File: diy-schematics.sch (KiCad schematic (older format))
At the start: 28 parts, among them J1 CAPSULE, J2 GAINCON, J3 AudioJack2_Ground, J4 USB_SOK, J5 USB_CON, J6 MIC_CON1, J7 MIC_CON2, U1 THAT1512PO8-U1, U2 NMA0515SC

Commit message: new PCB design, some minor compat changes in schematics
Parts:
- removed J3: AudioJack2_Ground, Connector_JST:JST_XH_B2B-XH-A_1x02_P2.50mm_Vertical, symbol Connector:AudioJack2_Ground
- added J3: AUDIO_JACK, Connector_JST:JST_XH_B3B-XH-A_1x03_P2.50mm_Vertical, symbol Connector:Conn_01x03_Female
- C1, C2, C8: footprint Capacitor_SMD:C_0805_2012Metric -> Capacitor_THT:CP_Radial_D5.0mm_P2.00mm
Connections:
- net Earth: now also J3.3 (Pin_3)
- net at C8.2: now also J3.1 (Pin_1), J3.2 (Pin_2)
- net at J4.2 (D-): now also J5.2 (Pin_2); no longer J5.3 (Pin_3)
- net at J4.3 (D+): now also J5.3 (Pin_3); no longer J5.2 (Pin_2)
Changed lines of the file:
@@
 F 0 "C1" V 3552 3950 50  0000 C CNN
 F 1 "22uF" V 3461 3950 50  0000 C CNN
-F 2 "Capacitor_SMD:C_0805_2012Metric" H 3338 3800 50  0001 C CNN
+F 2 "Capacitor_THT:CP_Radial_D5.0mm_P2.00mm" H 3338 3800 50  0001 C CNN
 F 3 "~" H 3300 3950 50  0001 C CNN
 	1    3300 3950
@@
 F 0 "C2" V 3552 4550 50  0000 C CNN
 F 1 "22uF" V 3461 4550 50  0000 C CNN
-F 2 "Capacitor_SMD:C_0805_2012Metric" H 3338 4400 50  0001 C CNN
+F 2 "Capacitor_THT:CP_Radial_D5.0mm_P2.00mm" H 3338 4400 50  0001 C CNN
 F 3 "~" H 3300 4550 50  0001 C CNN
 	1    3300 4550
@@
 F 0 "C8" V 6652 4100 50  0000 C CNN
 F 1 "22uF" V 6561 4100 50  0000 C CNN
-F 2 "Capacitor_SMD:C_0805_2012Metric" H 6438 3950 50  0001 C CNN
+F 2 "Capacitor_THT:CP_Radial_D5.0mm_P2.00mm" H 6438 3950 50  0001 C CNN
 F 3 "~" H 6400 4100 50  0001 C CNN
 	1    6400 4100
@@
 Wire Wire Line
 	3650 3950 4450 3950
-$Comp
-L Connector:AudioJack2_Ground J3
-U 1 1 61D2E7B1
-P 6800 4200
-F 0 "J3" H 6620 4218 50  0000 R CNN
-F 1 "AudioJack2_Ground" H 7050 4500 50  0000 R CNN
-F 2 "Connector_JST:JST_XH_B2B-XH-A_1x02_P2.50mm_Vertical" H 6800 4200 50  0001 C CNN
-F 3 "~" H 6800 4200 50  0001 C CNN
-	1    6800 4200
-	-1   0    0    -1
-$EndComp
 Wire Wire Line
 	6600 4100 6550 4100
@@
 $EndComp
 Wire Wire Line
-	10100 3850 10400 3850
-Wire Wire Line
-	10100 3950 10400 3950
-Wire Wire Line
 	9800 4450 10350 4450
 Wire Wire Line
@@
 	10100 3750 10350 3750
 Connection ~ 10350 3750
+Wire Wire Line
+	10100 3850 10200 3850
+Wire Wire Line
+	10200 3850 10300 3950
+Wire Wire Line
+	10300 3950 10400 3950
+Wire Wire Line
+	10100 3950 10200 3950
+Wire Wire Line
+	10200 3950 10300 3850
+Wire Wire Line
+	10300 3850 10400 3850
+$Comp
+L Connector:Conn_01x03_Female J3
+U 1 1 61D75578
+P 6800 4200
+F 0 "J3" H 6828 4226 50  0000 L CNN
+F 1 "AUDIO_JACK" H 6828 4135 50  0000 L CNN
+F 2 "Connector_JST:JST_XH_B3B-XH-A_1x03_P2.50mm_Vertical" H 6800 4200 50  0001 C CNN
+F 3 "~" H 6800 4200 50  0001 C CNN
+	1    6800 4200
+	1    0    0    -1
+$EndComp
+Wire Wire Line
+	6800 4400 6550 4400
+Wire Wire Line
+	6550 4400 6550 4300
+Wire Wire Line
+	6550 4300 6600 4300
 $EndSCHEMATC

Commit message: fixes to new PCB
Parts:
- removed J3: AUDIO_JACK, Connector_JST:JST_XH_B3B-XH-A_1x03_P2.50mm_Vertical, symbol Connector:Conn_01x03_Female
- added J3: Conn_01x02_Female, Connector_JST:JST_XH_B2B-XH-A_1x02_P2.50mm_Vertical, symbol Connector:Conn_01x02_Female
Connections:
- net Earth: now also J3.2 (Pin_2)
- net at C8.2: now also J3.1 (Pin_1)
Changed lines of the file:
@@
 Wire Wire Line
 	6600 4100 6550 4100
-Wire Wire Line
-	6600 4200 6550 4200
-Wire Wire Line
-	6550 4200 6550 4100
-Connection ~ 6550 4100
 $Comp
 L power:Earth #PWR0110
 U 1 1 61D34EC8
-P 6800 4500
-F 0 "#PWR0110" H 6800 4250 50  0001 C CNN
-F 1 "Earth" H 6800 4350 50  0001 C CNN
-F 2 "" H 6800 4500 50  0001 C CNN
-F 3 "~" H 6800 4500 50  0001 C CNN
-	1    6800 4500
-	1    0    0    -1
-$EndComp
-Wire Wire Line
-	6800 4500 6800 4400
+P 6800 4400
+F 0 "#PWR0110" H 6800 4150 50  0001 C CNN
+F 1 "Earth" H 6800 4250 50  0001 C CNN
+F 2 "" H 6800 4400 50  0001 C CNN
+F 3 "~" H 6800 4400 50  0001 C CNN
+	1    6800 4400
+	1    0    0    -1
+$EndComp
+Wire Wire Line
+	6800 4400 6800 4300
 Connection ~ 8650 4200
 Wire Wire Line
@@
 Wire Wire Line
 	10300 3850 10400 3850
-$Comp
-L Connector:Conn_01x03_Female J3
-U 1 1 61D75578
-P 6800 4200
-F 0 "J3" H 6828 4226 50  0000 L CNN
-F 1 "AUDIO_JACK" H 6828 4135 50  0000 L CNN
-F 2 "Connector_JST:JST_XH_B3B-XH-A_1x03_P2.50mm_Vertical" H 6800 4200 50  0001 C CNN
-F 3 "~" H 6800 4200 50  0001 C CNN
-	1    6800 4200
-	1    0    0    -1
-$EndComp
-Wire Wire Line
-	6800 4400 6550 4400
-Wire Wire Line
-	6550 4400 6550 4300
-Wire Wire Line
-	6550 4300 6600 4300
+Wire Wire Line
+	6800 4300 6550 4300
+Wire Wire Line
+	6550 4300 6550 4200
+Wire Wire Line
+	6550 4200 6600 4200
+$Comp
+L Connector:Conn_01x02_Female J3
+U 1 1 61D275D2
+P 6800 4100
+F 0 "J3" H 6828 4076 50  0000 L CNN
+F 1 "Conn_01x02_Female" H 6828 3985 50  0000 L CNN
+F 2 "Connector_JST:JST_XH_B2B-XH-A_1x02_P2.50mm_Vertical" H 6800 4100 50  0001 C CNN
+F 3 "~" H 6800 4100 50  0001 C CNN
+	1    6800 4100
+	1    0    0    -1
+$EndComp
 $EndSCHEMATC

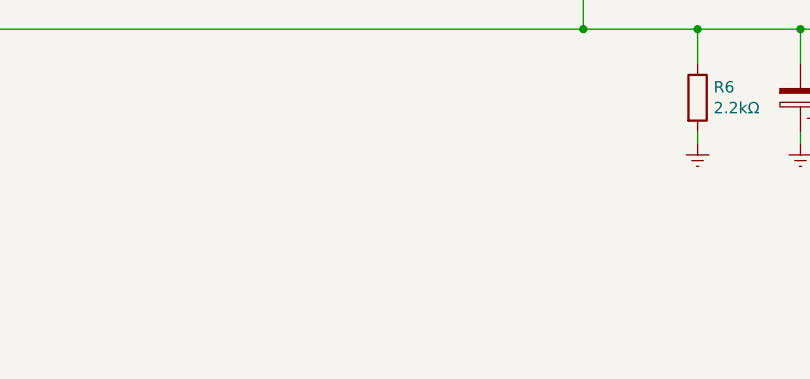
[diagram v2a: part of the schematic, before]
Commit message: added mounting holes, rendered gerber files
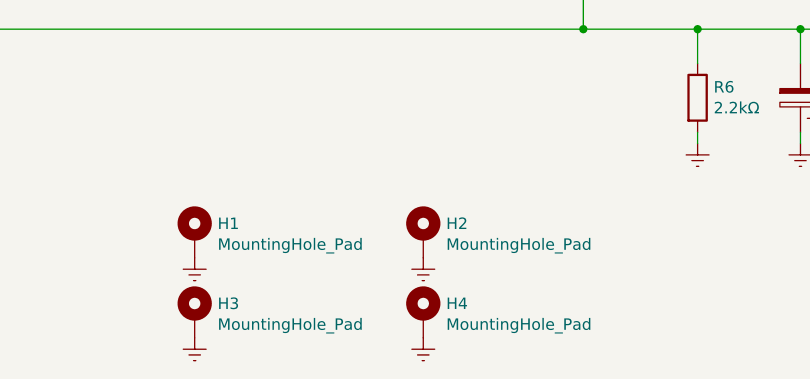
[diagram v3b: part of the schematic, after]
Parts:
- added H1, H2, H3, H4: MountingHole_Pad, MountingHole:MountingHole_2.2mm_M2_Pad, symbol Mechanical:MountingHole_Pad
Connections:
- net Earth: now also H1.1, H2.1, H3.1, H4.1
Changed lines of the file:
@@
+	1    0    0    -1
+$EndComp
+$Comp
+L Mechanical:MountingHole_Pad H1
+U 1 1 61D45B72
+P 3350 6750
+F 0 "H1" H 3450 6799 50  0000 L CNN
+F 1 "MountingHole_Pad" H 3450 6708 50  0000 L CNN
+F 2 "MountingHole:MountingHole_2.2mm_M2_Pad" H 3350 6750 50  0001 C CNN
+F 3 "~" H 3350 6750 50  0001 C CNN
+	1    3350 6750
+	1    0    0    -1
+$EndComp
+$Comp
+L power:Earth #PWR0106
+U 1 1 61D47E95
+P 3350 6850
+F 0 "#PWR0106" H 3350 6600 50  0001 C CNN
+F 1 "Earth" H 3350 6700 50  0001 C CNN
+F 2 "" H 3350 6850 50  0001 C CNN
+F 3 "~" H 3350 6850 50  0001 C CNN
+	1    3350 6850
+	1    0    0    -1
+$EndComp
+$Comp
+L Mechanical:MountingHole_Pad H3
+U 1 1 61D4BB30
+P 3350 7100
+F 0 "H3" H 3450 7149 50  0000 L CNN
+F 1 "MountingHole_Pad" H 3450 7058 50  0000 L CNN
+F 2 "MountingHole:MountingHole_2.2mm_M2_Pad" H 3350 7100 50  0001 C CNN
+F 3 "~" H 3350 7100 50  0001 C CNN
+	1    3350 7100
+	1    0    0    -1
+$EndComp
+$Comp
+L power:Earth #PWR0114
+U 1 1 61D4BB36
+P 3350 7200
+F 0 "#PWR0114" H 3350 6950 50  0001 C CNN
+F 1 "Earth" H 3350 7050 50  0001 C CNN
+F 2 "" H 3350 7200 50  0001 C CNN
+F 3 "~" H 3350 7200 50  0001 C CNN
+	1    3350 7200
+	1    0    0    -1
+$EndComp
+$Comp
+L Mechanical:MountingHole_Pad H2
+U 1 1 61D4EAF9
+P 4350 6750
+F 0 "H2" H 4450 6799 50  0000 L CNN
+F 1 "MountingHole_Pad" H 4450 6708 50  0000 L CNN
+F 2 "MountingHole:MountingHole_2.2mm_M2_Pad" H 4350 6750 50  0001 C CNN
+F 3 "~" H 4350 6750 50  0001 C CNN
+	1    4350 6750
+	1    0    0    -1
+$EndComp
+$Comp
+L power:Earth #PWR0115
+U 1 1 61D4EAFF
+P 4350 6850
+F 0 "#PWR0115" H 4350 6600 50  0001 C CNN
+F 1 "Earth" H 4350 6700 50  0001 C CNN
+F 2 "" H 4350 6850 50  0001 C CNN
+F 3 "~" H 4350 6850 50  0001 C CNN
+	1    4350 6850
+	1    0    0    -1
+$EndComp
+$Comp
+L Mechanical:MountingHole_Pad H4
+U 1 1 61D51962
+P 4350 7100
+F 0 "H4" H 4450 7149 50  0000 L CNN
+F 1 "MountingHole_Pad" H 4450 7058 50  0000 L CNN
+F 2 "MountingHole:MountingHole_2.2mm_M2_Pad" H 4350 7100 50  0001 C CNN
+F 3 "~" H 4350 7100 50  0001 C CNN
+	1    4350 7100
+	1    0    0    -1
+$EndComp
+$Comp
+L power:Earth #PWR0116
+U 1 1 61D51968
+P 4350 7200
+F 0 "#PWR0116" H 4350 6950 50  0001 C CNN
+F 1 "Earth" H 4350 7050 50  0001 C CNN
+F 2 "" H 4350 7200 50  0001 C CNN
+F 3 "~" H 4350 7200 50  0001 C CNN
+	1    4350 7200
 	1    0    0    -1
 $EndComp
